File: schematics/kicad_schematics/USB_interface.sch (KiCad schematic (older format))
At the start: 13 parts, among them Q1 NPN, Q2 NPN, U8 USB-TYPEB, U9 USBLC6-2P6

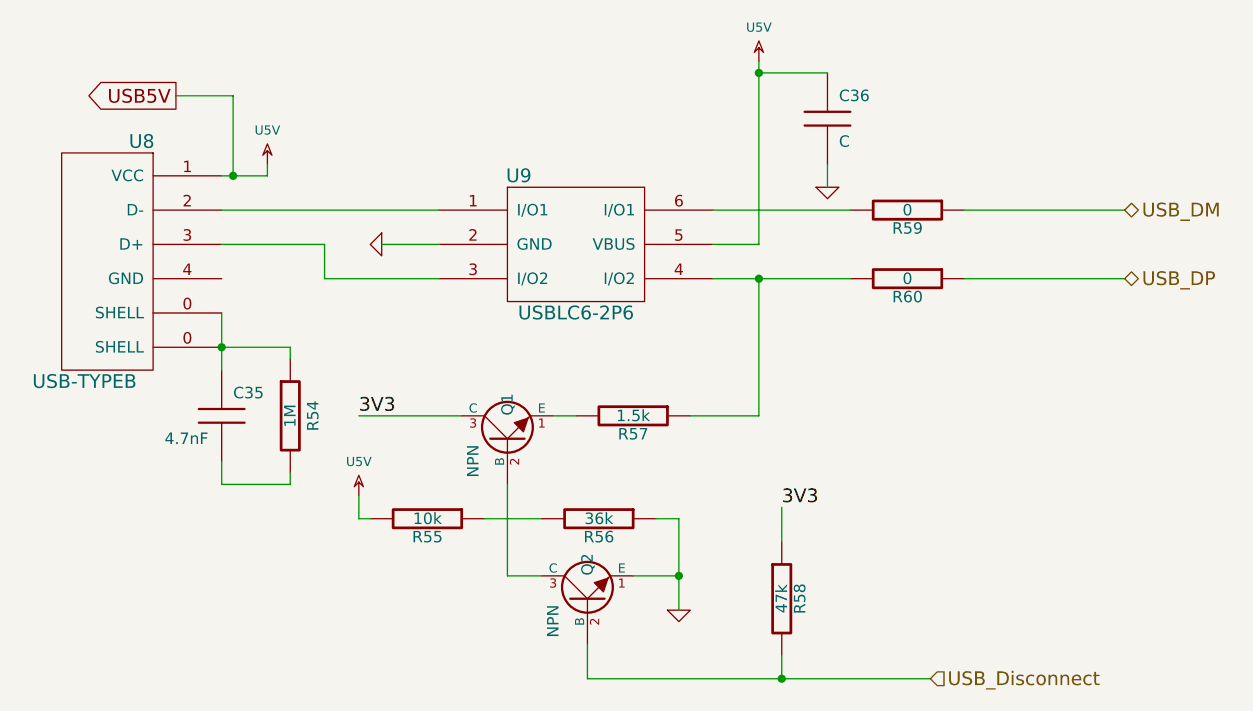
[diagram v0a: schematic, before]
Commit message: Updated USB connector to change the sheild pin to power input Updated the schematic to fix some schematic electrical issues
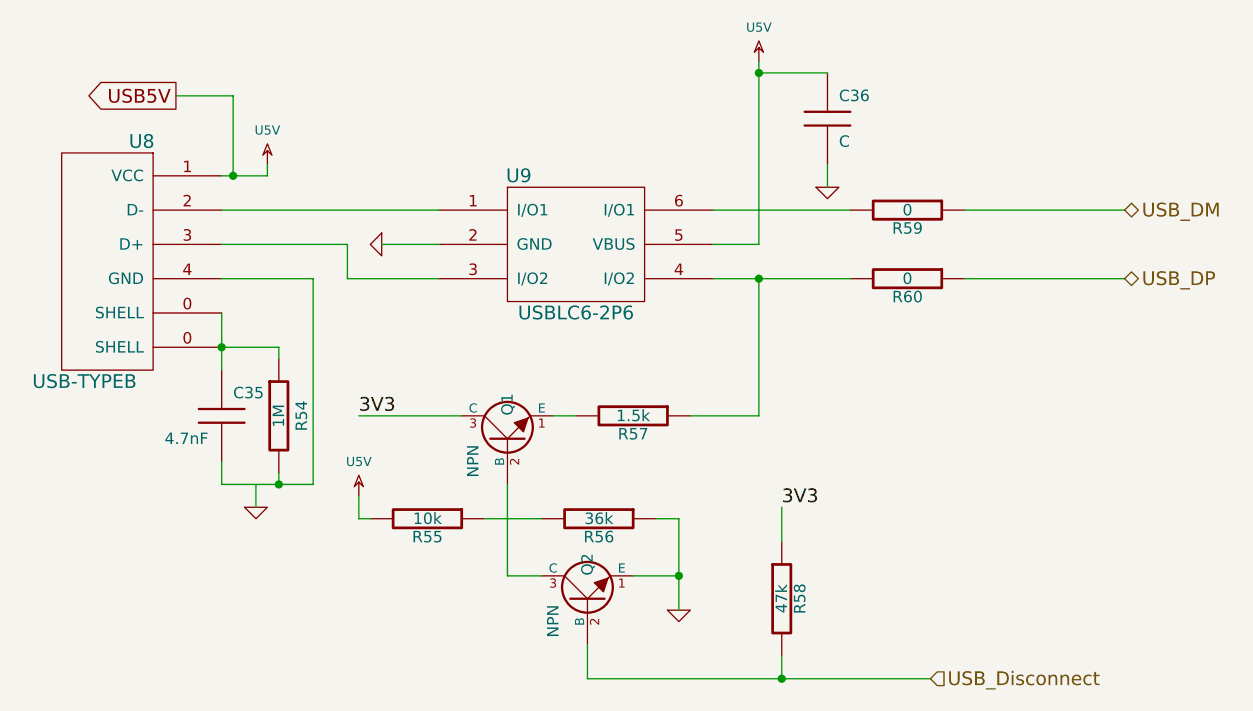
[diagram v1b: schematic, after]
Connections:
- net at U8.4 (GND): now also C35.2, R54.2
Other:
- moved on the sheet: R54
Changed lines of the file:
@@
-EESchema Schematic File Version 2  date Wed 10 Mar 2010 05:32:05 PM EST
+EESchema Schematic File Version 2  date Wed 10 Mar 2010 08:20:30 PM EST
 LIBS:power
 LIBS:device
@@
 Sheet 5 5
 Title ""
-Date "10 mar 2010"
+Date "11 mar 2010"
 Rev ""
 Comp ""
@@
 Comment4 ""
 $EndDescr
+Connection ~ 3750 4250
+Wire Wire Line
+	3900 4250 3500 4250
+Wire Wire Line
+	3900 4250 3900 3350
+Wire Wire Line
+	3900 3350 3500 3350
+Wire Wire Line
+	5950 4500 5950 4350
+Wire Wire Line
+	6600 5100 5100 5100
+Wire Wire Line
+	5100 5100 5100 4950
+Wire Wire Line
+	5300 4650 5500 4650
+Wire Wire Line
+	5500 4800 5500 4400
+Wire Wire Line
+	5500 4400 5400 4400
+Wire Wire Line
+	4650 4400 4900 4400
+Wire Wire Line
+	4100 3950 4550 3950
+Connection ~ 5850 3350
+Wire Wire Line
+	5850 3350 5850 3950
+Wire Wire Line
+	5850 3950 5550 3950
+Connection ~ 5850 2450
+Wire Wire Line
+	6150 2450 5850 2450
+Wire Wire Line
+	7450 3050 6750 3050
+Wire Wire Line
+	6250 3050 5650 3050
+Wire Wire Line
+	5650 3200 5850 3200
+Wire Wire Line
+	4450 3350 4050 3350
+Wire Wire Line
+	4050 3350 4050 3200
+Wire Wire Line
+	4050 3200 3500 3200
+Wire Wire Line
+	4450 3200 4200 3200
+Wire Wire Line
+	3500 3500 3500 3750
+Wire Wire Line
+	3500 4250 3500 4150
+Wire Wire Line
+	3750 4250 3750 4200
+Wire Wire Line
+	3500 3650 3750 3650
+Wire Wire Line
+	3750 3650 3750 3700
+Connection ~ 3500 3650
+Wire Wire Line
+	4450 3050 3500 3050
+Wire Wire Line
+	3500 2900 3700 2900
+Wire Wire Line
+	3700 2900 3700 2850
+Wire Wire Line
+	6250 3350 5650 3350
+Wire Wire Line
+	6750 3350 7450 3350
+Wire Wire Line
+	6150 2850 6150 2950
+Wire Wire Line
+	5850 3200 5850 2400
+Wire Wire Line
+	5050 3950 4950 3950
+Wire Wire Line
+	4100 4300 4100 4400
+Wire Wire Line
+	4100 4400 4150 4400
+Wire Wire Line
+	4750 4250 4750 4650
+Wire Wire Line
+	4750 4650 4900 4650
+Connection ~ 5500 4650
+Wire Wire Line
+	5950 5000 5950 5100
+Connection ~ 5950 5100
+Wire Wire Line
+	3300 2550 3550 2550
+Wire Wire Line
+	3550 2550 3550 2900
 Connection ~ 3550 2900
 Wire Wire Line
-	3550 2900 3550 2550
-Wire Wire Line
-	3550 2550 3300 2550
-Connection ~ 5950 5100
-Wire Wire Line
-	5950 5000 5950 5100
-Connection ~ 5500 4650
-Wire Wire Line
-	4900 4650 4750 4650
-Wire Wire Line
-	4750 4650 4750 4250
-Wire Wire Line
-	4150 4400 4100 4400
-Wire Wire Line
-	4100 4400 4100 4300
-Wire Wire Line
-	5050 3950 4950 3950
-Wire Wire Line
-	5850 2400 5850 3200
-Wire Wire Line
-	6150 2850 6150 2950
-Wire Wire Line
-	6750 3350 7450 3350
-Wire Wire Line
-	5650 3350 6250 3350
-Wire Wire Line
-	3700 2850 3700 2900
-Wire Wire Line
-	3700 2900 3500 2900
-Wire Wire Line
-	4450 3050 3500 3050
-Connection ~ 3500 3650
-Wire Wire Line
-	3800 3700 3800 3650
-Wire Wire Line
-	3800 3650 3500 3650
-Wire Wire Line
-	3800 4200 3800 4250
-Wire Wire Line
-	3800 4250 3500 4250
-Wire Wire Line
-	3500 4250 3500 4150
-Wire Wire Line
-	3500 3750 3500 3500
-Wire Wire Line
-	4450 3200 4200 3200
-Wire Wire Line
-	3500 3200 3950 3200
-Wire Wire Line
-	3950 3200 3950 3350
-Wire Wire Line
-	3950 3350 4450 3350
-Wire Wire Line
-	5850 3200 5650 3200
-Wire Wire Line
-	6250 3050 5650 3050
-Wire Wire Line
-	7450 3050 6750 3050
-Wire Wire Line
-	6150 2450 5850 2450
-Connection ~ 5850 2450
-Wire Wire Line
-	5550 3950 5850 3950
-Wire Wire Line
-	5850 3950 5850 3350
-Connection ~ 5850 3350
-Wire Wire Line
-	4100 3950 4550 3950
-Wire Wire Line
-	4650 4400 4900 4400
-Wire Wire Line
-	5400 4400 5500 4400
-Wire Wire Line
-	5500 4400 5500 4800
-Wire Wire Line
-	5300 4650 5500 4650
-Wire Wire Line
-	5100 4950 5100 5100
-Wire Wire Line
-	5100 5100 6600 5100
-Wire Wire Line
-	5950 4500 5950 4350
+	3650 4250 3650 4350
+$Comp
+L GND #PWR055
+U 1 1 4B9843F1
+P 3650 4350
+F 0 "#PWR055" H 3650 4350 30  0001 C CNN
+F 1 "GND" H 3650 4280 30  0001 C CNN
+	1    3650 4350
+	1    0    0    -1
+$EndComp
 Text GLabel 3300 2550 0    60   Output ~ 0
 USB5V
@@
 $EndComp
 $Comp
-L 3V3 #PWR054
+L 3V3 #PWR056
 U 1 1 4B7E9511
 P 4100 4300
-F 0 "#PWR054" H 4100 4400 40  0001 C CNN
+F 0 "#PWR056" H 4100 4400 40  0001 C CNN
 F 1 "U5V" H 4100 4449 40  0000 C CNN
 	1    4100 4300
@@
 $EndComp
 $Comp
-L GND #PWR055
+L GND #PWR057
 U 1 1 4B7E94D3
 P 6150 2950
-F 0 "#PWR055" H 6150 2950 30  0001 C CNN
+F 0 "#PWR057" H 6150 2950 30  0001 C CNN
 F 1 "GND" H 6150 2880 30  0001 C CNN
 	1    6150 2950
@@
 $EndComp
 $Comp
-L 3V3 #PWR056
+L 3V3 #PWR058
 U 1 1 4B7E945B
 P 5850 2400
-F 0 "#PWR056" H 5850 2500 40  0001 C CNN
+F 0 "#PWR058" H 5850 2500 40  0001 C CNN
 F 1 "U5V" H 5850 2549 40  0000 C CNN
 	1    5850 2400
@@
 $EndComp
 $Comp
-L GND #PWR057
+L GND #PWR059
 U 1 1 4B7E9432
 P 5500 4800
-F 0 "#PWR057" H 5500 4800 30  0001 C CNN
+F 0 "#PWR059" H 5500 4800 30  0001 C CNN
 F 1 "GND" H 5500 4730 30  0001 C CNN
 	1    5500 4800
@@
 L R R54
 U 1 1 4B7E93E4
-P 3800 3950
-F 0 "R54" V 3900 3950 50  0000 C CNN
-F 1 "1M" V 3800 3950 50  0000 C CNN
-	1    3800 3950
+P 3750 3950
+F 0 "R54" V 3850 3950 50  0000 C CNN
+F 1 "1M" V 3750 3950 50  0000 C CNN
+	1    3750 3950
 	1    0    0    -1
 $EndComp
@@
 $EndComp
 $Comp
-L 3V3 #PWR058
+L 3V3 #PWR060
 U 1 1 4B7E93C0
 P 3700 2850
-F 0 "#PWR058" H 3700 2950 40  0001 C CNN
+F 0 "#PWR060" H 3700 2950 40  0001 C CNN
 F 1 "U5V" H 3700 2999 40  0000 C CNN
 	1    3700 2850
@@
 $EndComp
 $Comp
-L GND #PWR059
+L GND #PWR061
 U 1 1 4B7E92CC
 P 4200 3200
-F 0 "#PWR059" H 4200 3200 30  0001 C CNN
+F 0 "#PWR061" H 4200 3200 30  0001 C CNN
 F 1 "GND" H 4200 3130 30  0001 C CNN
 	1    4200 3200

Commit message: back annotated footprints into eeschem schematic
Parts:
- C35, C36, R54, R55, R56, R57, R58, R59, R60: footprint (none) -> SM0805
- U8: footprint (none) -> mini-usb-b
- U9: footprint (none) -> SOT23_6L
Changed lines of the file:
@@
-EESchema Schematic File Version 2  date Wed 10 Mar 2010 08:20:30 PM EST
+EESchema Schematic File Version 2  date Fri 12 Mar 2010 11:31:07 AM EST
 LIBS:power
 LIBS:device
@@
 F 0 "R58" V 6030 4750 50  0000 C CNN
 F 1 "47k" V 5950 4750 50  0000 C CNN
+F 2 "SM0805" H 5950 4750 60  0001 C CNN
 	1    5950 4750
 	1    0    0    -1
@@
 F 0 "R55" V 4480 4400 50  0000 C CNN
 F 1 "10k" V 4400 4400 50  0000 C CNN
+F 2 "SM0805" H 4400 4400 60  0001 C CNN
 	1    4400 4400
 	0    1    1    0
@@
 F 0 "R56" V 5230 4400 50  0000 C CNN
 F 1 "36k" V 5150 4400 50  0000 C CNN
+F 2 "SM0805" H 5150 4400 60  0001 C CNN
 	1    5150 4400
 	0    1    1    0
@@
 F 0 "R57" V 5380 3950 50  0000 C CNN
 F 1 "1.5k" V 5300 3950 50  0000 C CNN
+F 2 "SM0805" H 5300 3950 60  0001 C CNN
 	1    5300 3950
 	0    1    1    0
@@
 F 0 "C36" H 6200 2750 50  0000 L CNN
 F 1 "C" H 6200 2550 50  0000 L CNN
+F 2 "SM0805" H 6150 2650 60  0001 C CNN
 	1    6150 2650
 	1    0    0    -1
@@
 F 0 "R60" V 6580 3350 50  0000 C CNN
 F 1 "0" V 6500 3350 50  0000 C CNN
+F 2 "SM0805" H 6500 3350 60  0001 C CNN
 	1    6500 3350
 	0    1    1    0
@@
 F 0 "R59" V 6580 3050 50  0000 C CNN
 F 1 "0" V 6500 3050 50  0000 C CNN
+F 2 "SM0805" H 6500 3050 60  0001 C CNN
 	1    6500 3050
 	0    1    1    0
@@
 F 0 "R54" V 3850 3950 50  0000 C CNN
 F 1 "1M" V 3750 3950 50  0000 C CNN
+F 2 "SM0805" H 3750 3950 60  0001 C CNN
 	1    3750 3950
 	1    0    0    -1
@@
 F 0 "C35" H 3550 4050 50  0000 L CNN
 F 1 "4.7nF" H 3250 3850 50  0000 L CNN
+F 2 "SM0805" H 3500 3950 60  0001 C CNN
 	1    3500 3950
 	1    0    0    -1
@@
 F 0 "U9" H 4800 3500 60  0000 C CNN
 F 1 "USBLC6-2P6" H 5050 2900 60  0000 C CNN
+F 2 "SOT23_6L" H 5050 3200 60  0001 C CNN
 	1    5050 3200
 	1    0    0    -1
@@
 F 0 "U8" H 3050 3650 60  0000 C CNN
 F 1 "USB-TYPEB" H 3300 2600 60  0000 C CNN
+F 2 "mini-usb-b" H 3100 3200 60  0001 C CNN
 	1    3100 3200
 	-1   0    0    -1

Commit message: added datasheets and modified schematic components for new dip switches
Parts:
- Q1, Q2: footprint (none) -> -SOT23; Part (none) -> BC847_BC547
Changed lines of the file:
@@
-EESchema Schematic File Version 2  date Sat 13 Mar 2010 04:13:45 PM EST
+EESchema Schematic File Version 2  date Sun 14 Mar 2010 12:34:26 PM EDT
 LIBS:power
 LIBS:device
@@
 Sheet 5 5
 Title ""
-Date "13 mar 2010"
+Date "14 mar 2010"
 Rev ""
 Comp ""
@@
 	3650 4250 3650 4350
 $Comp
-L GND #PWR055
+L GND #PWR054
 U 1 1 4B9843F1
 P 3650 4350
-F 0 "#PWR055" H 3650 4350 30  0001 C CNN
+F 0 "#PWR054" H 3650 4350 30  0001 C CNN
 F 1 "GND" H 3650 4280 30  0001 C CNN
 	1    3650 4350
@@
 $EndComp
 $Comp
-L 3V3 #PWR056
+L 3V3 #PWR055
 U 1 1 4B7E9511
 P 4100 4300
-F 0 "#PWR056" H 4100 4400 40  0001 C CNN
+F 0 "#PWR055" H 4100 4400 40  0001 C CNN
 F 1 "U5V" H 4100 4449 40  0000 C CNN
 	1    4100 4300
@@
 F 0 "Q2" H 5250 4750 50  0000 C CNN
 F 1 "NPN" H 5002 4900 50  0000 C CNN
+F 2 "-SOT23" H 5100 4750 60  0001 C CNN
+F 4 "BC847_BC547" H 5100 4750 60  0001 C CNN "Part"
 	1    5100 4750
 	0    -1   -1   0
 $EndComp
 $Comp
-L GND #PWR057
+L GND #PWR056
 U 1 1 4B7E94D3
 P 6150 2950
-F 0 "#PWR057" H 6150 2950 30  0001 C CNN
+F 0 "#PWR056" H 6150 2950 30  0001 C CNN
 F 1 "GND" H 6150 2880 30  0001 C CNN
 	1    6150 2950
@@
 F 0 "Q1" H 4900 4050 50  0000 C CNN
 F 1 "NPN" H 4652 4200 50  0000 C CNN
+F 2 "-SOT23" H 4750 4050 60  0001 C CNN
+F 4 "BC847_BC547" H 4750 4050 60  0001 C CNN "Part"
 	1    4750 4050
 	0    -1   -1   0
@@
 $EndComp
 $Comp
-L 3V3 #PWR058
+L 3V3 #PWR057
 U 1 1 4B7E945B
 P 5850 2400
-F 0 "#PWR058" H 5850 2500 40  0001 C CNN
+F 0 "#PWR057" H 5850 2500 40  0001 C CNN
 F 1 "U5V" H 5850 2549 40  0000 C CNN
 	1    5850 2400
@@
 $EndComp
 $Comp
-L GND #PWR059
+L GND #PWR058
 U 1 1 4B7E9432
 P 5500 4800
-F 0 "#PWR059" H 5500 4800 30  0001 C CNN
+F 0 "#PWR058" H 5500 4800 30  0001 C CNN
 F 1 "GND" H 5500 4730 30  0001 C CNN
 	1    5500 4800
@@
 $EndComp
 $Comp
-L 3V3 #PWR060
+L 3V3 #PWR059
 U 1 1 4B7E93C0
 P 3700 2850
-F 0 "#PWR060" H 3700 2950 40  0001 C CNN
+F 0 "#PWR059" H 3700 2950 40  0001 C CNN
 F 1 "U5V" H 3700 2999 40  0000 C CNN
 	1    3700 2850
@@
 $EndComp
 $Comp
-L GND #PWR061
+L GND #PWR060
 U 1 1 4B7E92CC
 P 4200 3200
-F 0 "#PWR061" H 4200 3200 30  0001 C CNN
+F 0 "#PWR060" H 4200 3200 30  0001 C CNN
 F 1 "GND" H 4200 3130 30  0001 C CNN
 	1    4200 3200
